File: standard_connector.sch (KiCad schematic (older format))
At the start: 0 parts

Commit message: power updated still need to add underpad also changed input connector to 5 pin and added fuses, added current sense with op-amp for solinoids
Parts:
- added P?: CONN_5, symbol CONN_5
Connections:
- new net 12V: P?.2
- new net CANH: P?.3
- new net CANL: P?.4
- new net GND: P?.5
- new net PWR_SOL_IN: P?.1
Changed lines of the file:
@@
-EESchema Schematic File Version 2  date 4/15/2013 1:22:57 AM
+EESchema Schematic File Version 2  date 4/16/2013 12:48:50 AM
 LIBS:power
 LIBS:device
@@
 LIBS:pinball_components
 LIBS:micro-controller
+LIBS:CurrentSense
+LIBS:pinball-power
 LIBS:base-module-cache
 EELAYER 27 0
@@
 $Descr A4 11693 8268
 encoding utf-8
-Sheet 7 7
+Sheet 8 8
 Title ""
-Date "15 apr 2013"
+Date "16 apr 2013"
 Rev ""
 Comp ""
@@
 Comment4 ""
 $EndDescr
+Text HLabel 4950 2150 2    60   Output ~ 0
+PWR_SOL_IN
+Text HLabel 4950 2250 2    60   Output ~ 0
+12V
+Text HLabel 4950 2350 2    60   BiDi ~ 0
+CANH
+Text HLabel 4950 2450 2    60   BiDi ~ 0
+CANL
+Wire Wire Line
+	4950 2450 3450 2450
+Wire Wire Line
+	4950 2350 3450 2350
+Wire Wire Line
+	3450 2250 4950 2250
+Wire Wire Line
+	3450 2150 4950 2150
+$Comp
+L CONN_5 P?
+U 1 1 516CDA4B
+P 3050 2350
+F 0 "P?" V 3000 2350 50  0000 C CNN
+F 1 "CONN_5" V 3100 2350 50  0000 C CNN
+F 2 "" H 3050 2350 60  0000 C CNN
+F 3 "" H 3050 2350 60  0000 C CNN
+	1    3050 2350
+	-1   0    0    -1
+$EndComp
+$Comp
+L GND #PWR?
+U 1 1 516CDA73
+P 3500 2600
+F 0 "#PWR?" H 3500 2600 30  0001 C CNN
+F 1 "GND" H 3500 2530 30  0001 C CNN
+F 2 "" H 3500 2600 60  0000 C CNN
+F 3 "" H 3500 2600 60  0000 C CNN
+	1    3500 2600
+	1    0    0    -1
+$EndComp
+Wire Wire Line
+	3500 2600 3500 2550
+Wire Wire Line
+	3500 2550 3450 2550
 $EndSCHEMATC

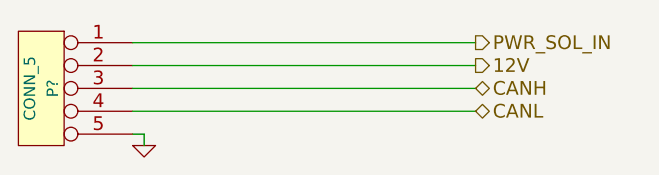
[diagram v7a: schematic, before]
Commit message: changed the controller adding some shift registers
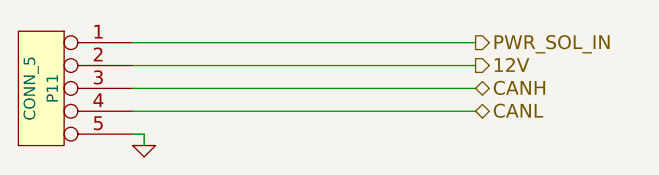
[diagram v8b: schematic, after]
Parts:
- gave numbers to parts that had none: 1
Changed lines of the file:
@@
-EESchema Schematic File Version 2  date 4/16/2013 9:07:53 PM
+EESchema Schematic File Version 2  date 4/17/2013 1:22:00 AM
 LIBS:power
 LIBS:device
@@
 LIBS:pinball-power
 LIBS:dips-s
+LIBS:Gajda_cmosieee
+LIBS:Gajda_ttlieee
 LIBS:base-module-cache
 EELAYER 27 0
@@
 	3450 2150 4950 2150
 $Comp
-L CONN_5 P?
+L CONN_5 P11
 U 1 1 516CDA4B
 P 3050 2350
-F 0 "P?" V 3000 2350 50  0000 C CNN
+F 0 "P11" V 3000 2350 50  0000 C CNN
 F 1 "CONN_5" V 3100 2350 50  0000 C CNN
 F 2 "" H 3050 2350 60  0000 C CNN
@@
 $EndComp
 $Comp
-L GND #PWR?
+L GND #PWR40
 U 1 1 516CDA73
 P 3500 2600
-F 0 "#PWR?" H 3500 2600 30  0001 C CNN
+F 0 "#PWR40" H 3500 2600 30  0001 C CNN
 F 1 "GND" H 3500 2530 30  0001 C CNN
 F 2 "" H 3500 2600 60  0000 C CNN
